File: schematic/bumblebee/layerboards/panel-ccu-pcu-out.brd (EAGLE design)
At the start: 85 x 100 mm, 49 parts, among them P1 B3B-EH-A, Q1 IRF9530, Q10 IRF9530, Q2 IRF9530, Q3 IRF9530, Q5 IRF9530, Q7 IRF9530, T1 2N7002E, T2 2N7002E, T3 2N7002E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

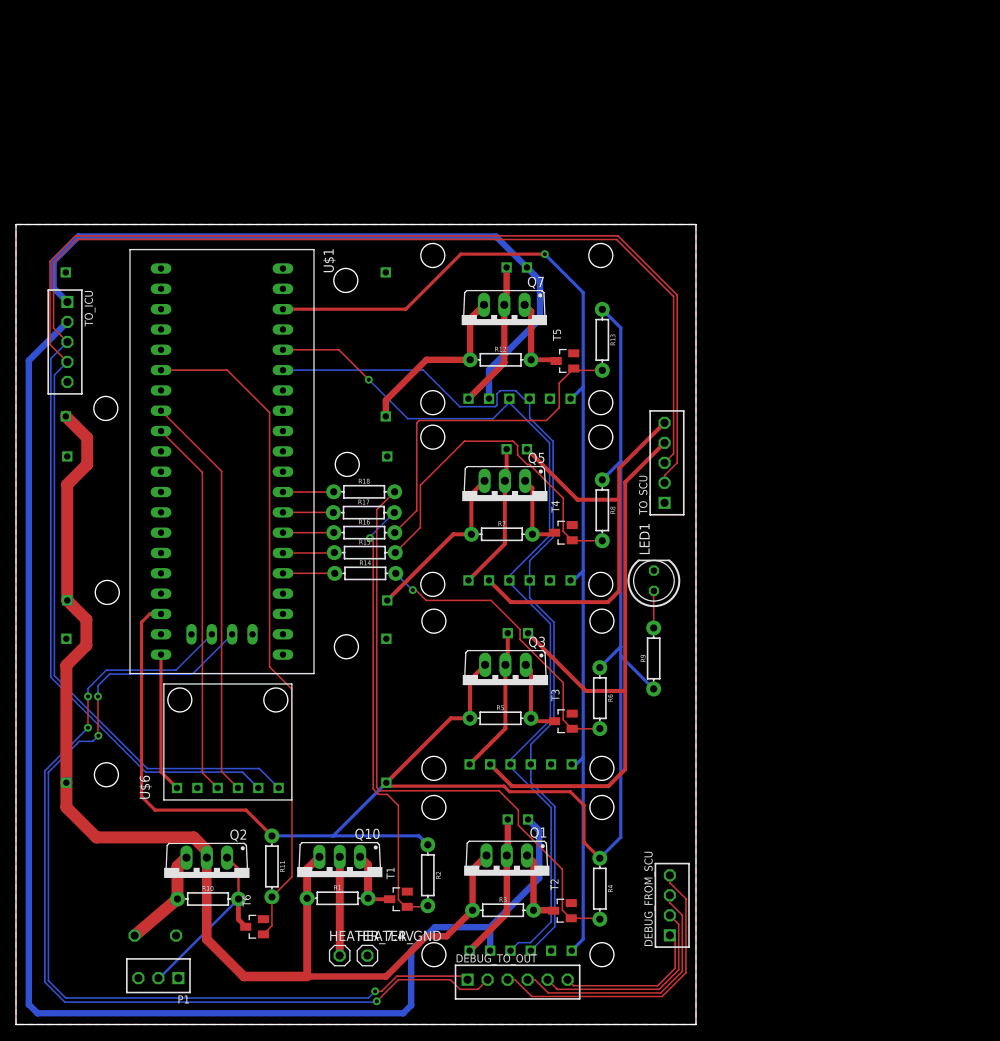
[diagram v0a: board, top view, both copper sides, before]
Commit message: Все платы готовы и отправлены в резонит
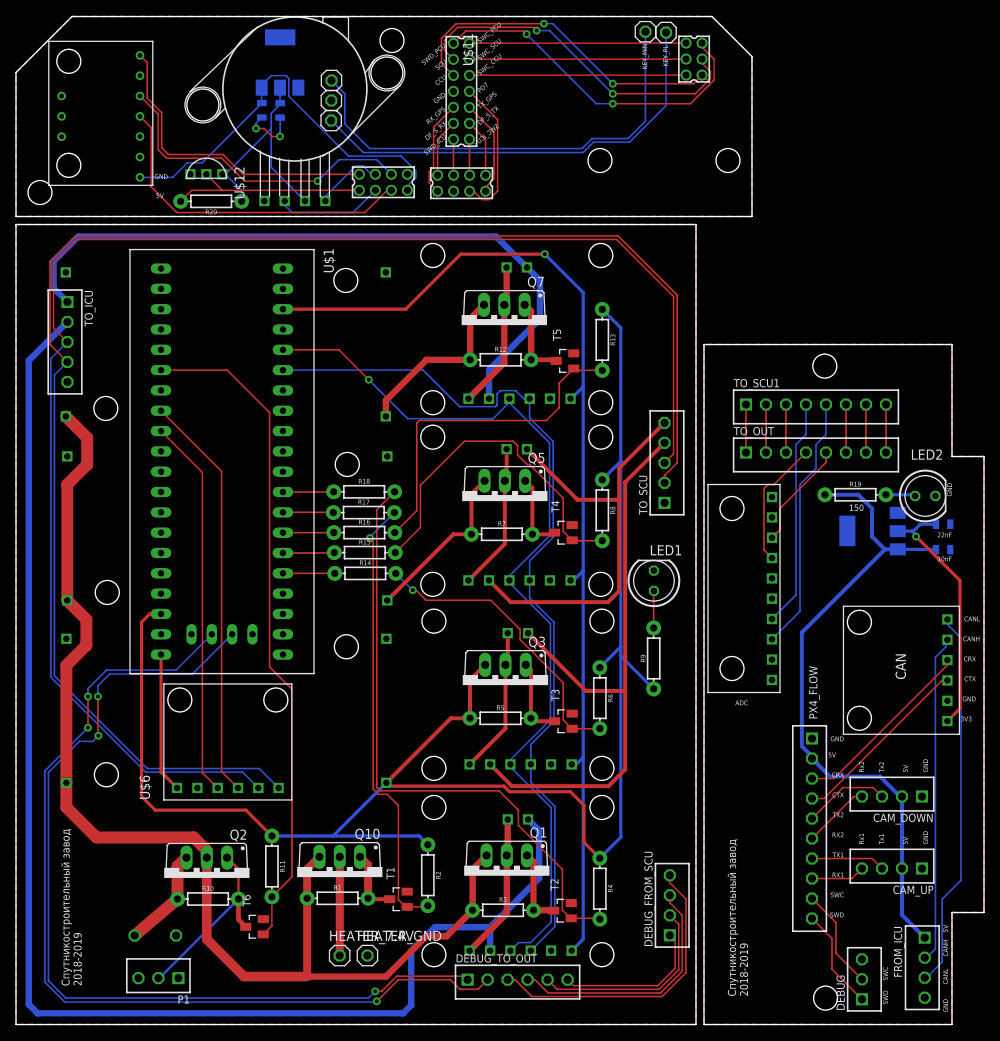
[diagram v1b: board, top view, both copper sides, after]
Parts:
- added C1, C3: 22uF, SparkFun-Capacitors:0805
- added C2, C4: 10uF, SparkFun-Capacitors:0805
- added CAM_DOWN, CAM_UP, FROM_ICU: B4B-EH-A, con-jst-eh:B4B-EH-A
- added CAN: CAN, bluepill:CAN
- added DEBUG: B3B-EH-A, con-jst-eh:B3B-EH-A
- added IC1, LDO: REG1117, burr-brown:SOT223
- added JP1, JP2, JP6, JP7, JP8: (no value), pinhead:1X01
- added LED2: (no value), led:LED5MM
- added PX4_FLOW: B10B-EH-A, con-jst-eh:B10B-EH-A
- added R19: 150, SparkFun-Resistors:AXIAL-0.3
- added R20: 4k7, SparkFun-Resistors:AXIAL-0.3
- added TO_OUT, TO_SCU1: B8B-EH-A, con-jst-eh:B8B-EH-A
- added U$10: ADS, bluepill:ADS
- added U$11: MPX, bluepill:MPX
- added U$12: TEMP, bluepill:TEMP
- added U$13: LSM303C, bluepill:LSM303C
- added X1: 332-14, con-garry:332-14
- added X2, X3: 332-08, con-garry:332-08
- added X4: 332-06, con-garry:332-06
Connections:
- new net 3V1: C1.1, CAN.3V3, LDO.2
- new net 3V2: C3.1, IC1.2, R20.P$1, U$11.VCC, U$12.VDD
- new net 5V: C4.1, IC1.3, U$13.5V, X2.7
- new net 5V_CCU1: C2.1, CAM_DOWN.2, CAM_UP.2, FROM_ICU.1, LDO.3, PX4_FLOW.2, R19.P$1
- new net ADC_1: U$11.V1, X2.3
- new net ADC_2: U$11.V2, X2.4
- new net CRX: CAN.CRX, PX4_FLOW.3
- new net CTX: CAN.CTX, PX4_FLOW.4
- new net DF_S_RX: X1.4, X3.2
- new net DF_S_TX: X1.3, X3.8
- new net DQ: R20.P$2, U$12.DQ, X2.1
- new net GND1: C1.2, C2.2, CAM_DOWN.1, CAM_UP.1, CAN.GND, FROM_ICU.4, LDO.1, LED2.K, PX4_FLOW.1
- new net GND2: C3.2, C4.2, IC1.1, JP7.1, U$11.GND, U$12.GND, U$13.GND, X1.8, X2.8, X3.3
- new net KEY_MINUS: JP1.1, JP6.1
- new net KEY_PLUS: JP2.1, JP8.1
- new net MAG_CS: U$13.CSM, X2.2
- new net N$23: CAN.CANL, FROM_ICU.3
- new net N$24: CAN.CANH, FROM_ICU.2
- new net N$25: LED2.A, R19.P$2
- new net N$26: TO_OUT.8, TO_SCU1.8
- new net N$27: TO_OUT.7, TO_SCU1.7
- new net N$28: TO_OUT.6, TO_SCU1.6
- new net N$29: TO_OUT.3, TO_SCU1.3
- new net N$30: TO_OUT.2, TO_SCU1.2
- new net N$31: TO_OUT.1, TO_SCU1.1
- new net N$32: TO_SCU1.5, U$10.SCL
- new net N$33: TO_SCU1.4, U$10.SDA
- new net N$34: TO_OUT.5, U$10.A1
- new net N$35: TO_OUT.4, U$10.A0
- new net PD7: X1.7, X3.5
- new net RX1: CAM_UP.4, PX4_FLOW.8
- new net RX2: CAM_DOWN.4, PX4_FLOW.6
- new net RX_GPS: X1.6, X3.1
- new net SCL: U$13.SCL, X2.5
- new net SDA: U$13.SDA, X2.6
- new net SWC: DEBUG.2, PX4_FLOW.9
- new net SWCLK_CCU: X1.9, X4.2
- new net SWCLK_PCU: X1.13, X4.6
- new net SWCLK_SCU: X1.11, X4.4
- new net SWC_ICU: X1.1, X3.6
- new net SWD: DEBUG.1, PX4_FLOW.10
- new net SWDIO_CCU: X1.10, X4.1
- new net SWDIO_PCU: X1.14, X4.5
- new net SWDIO_SCU: X1.12, X4.3
- new net SWD_ICU: X1.2, X3.4
- new net TX1: CAM_UP.3, PX4_FLOW.7
- new net TX2: CAM_DOWN.3, PX4_FLOW.5
- new net TX_GPS: X1.5, X3.7
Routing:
- net 5V_CCU1: track 0.00 -> 81.8 mm
- net KEY_PLUS: track 0.00 -> 57.6 mm
- net KEY_MINUS: track 0.00 -> 55.1 mm
- net 5V: track 0.00 -> 50.1 mm
- net N$23: track 0.00 -> 47.5 mm
- net SWDIO_SCU: track 0.00 -> 43.8 mm, vias 0 -> 2
- net SWDIO_PCU: track 0.00 -> 43.5 mm, vias 0 -> 2
- net SWDIO_CCU: track 0.00 -> 42.1 mm, vias 0 -> 2
- net SCL: track 0.00 -> 41.9 mm
- net N$24: track 0.00 -> 41.1 mm
- net SDA: track 0.00 -> 40.3 mm, vias 0 -> 1
- net MAG_CS: track 0.00 -> 38.7 mm
- net N$32: track 0.00 -> 32.1 mm
- net 3V1: track 0.00 -> 32.0 mm, vias 0 -> 1
- net 3V2: track 0.00 -> 29.1 mm
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- added copper zone on layer 1, net GND1
- added copper zone on layer 16, net GND1
- added copper zone on layer 1, net GND2
- added copper zone on layer 16, net GND2
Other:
- board size 85 x 100 mm -> 121 x 126 mm
- board text added: "10nF"
- board text added: "150"
- board text added: "22nF"
- board text added: "3V3"
- board text added: "5V"
- board text added: "ADC"
- board text added: "ADC_1"
- board text added: "ADC_2"
- board text added: "CANH"
- board text added: "CANL"
- board text added: "CCU"
- board text added: "CRX"
- board text added: "CTX"
- board text added: "DF_S_RX"
- board text added: "DF_S_TX"
- board text added: "DQ"
- board text added: "GND"
- board text added: "KEY_MIN"
- board text added: "KEY_PL"
- board text added: "MAG_CS"
- board text added: "PD7"
- board text added: "RX1"
- board text added: "RX2"
- board text added: "RX_GPS"
- board text added: "Rx1"
- board text added: "Rx2"
- board text added: "SCL"
- board text added: "SCU"
- board text added: "SDA"
- board text added: "SWC"
- board text added: "SWC_CCU"
- board text added: "SWC_ICU"
- board text added: "SWC_PCU"
- board text added: "SWC_SCU"
- board text added: "SWD"
- board text added: "SWD_ICU"
- board text added: "SWD_PCU"
- board text added: "SWD_SCU"
- board text added: "TX1"
- board text added: "TX2"
- board text added: "TX_GPS"
- board text added: "Tx1"
- board text added: "Tx2"
- board text added: "Спутникостроительный завод 2018-2019"
